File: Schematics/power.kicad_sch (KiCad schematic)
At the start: 6 parts, among them U3 PowerIn, U4 LDL1117-3.3

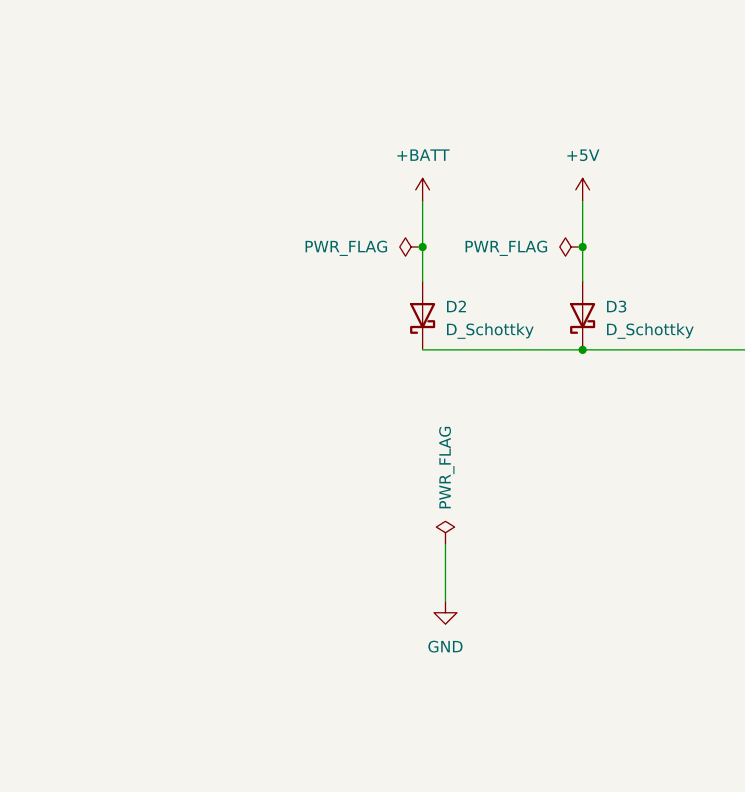
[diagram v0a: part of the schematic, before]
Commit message: added aux pyro added reverse polarity protection re routed just need to clean up and check pin assignments
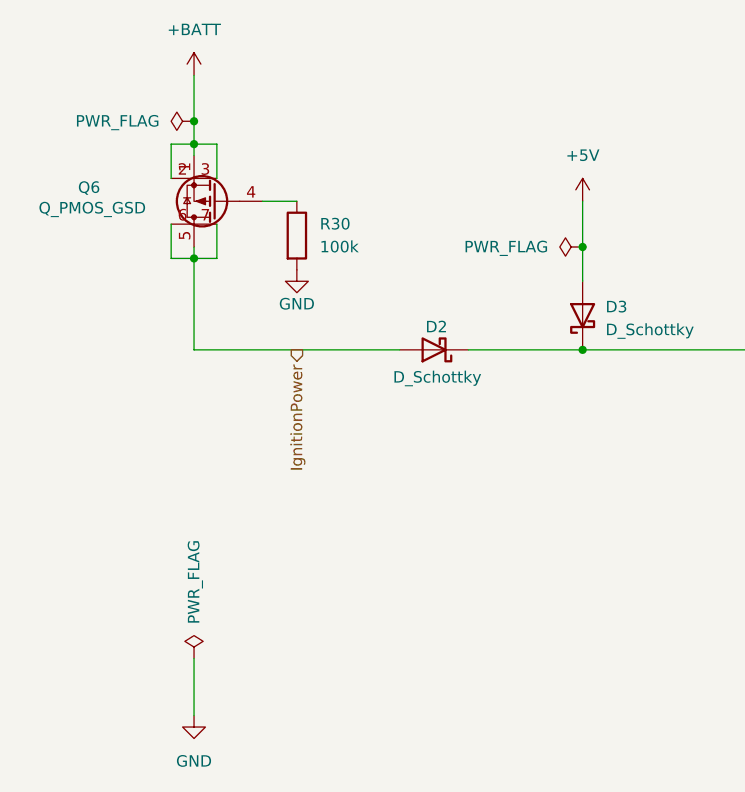
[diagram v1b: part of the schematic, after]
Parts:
- added Q6: Q_PMOS_GSD, myFootprints:SOIC127P599X175-8N, symbol Transistor_FET:Q_PMOS_SGD
- added R30: 100k, Resistor_SMD:R_0805_2012Metric_Pad1.20x1.40mm_HandSolder, symbol Device:R
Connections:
- net +BATT: now also Q6.1 (S), Q6.2 (Source), Q6.3 (Source); no longer D2.2 (A)
- net GND: now also R30.2
- new net: Q6.4 (G), R30.1
- new net IgnitionPower: D2.2 (A), Q6.5 (D), Q6.6 (Drain), Q6.7 (Drain)
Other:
- moved on the sheet: D2

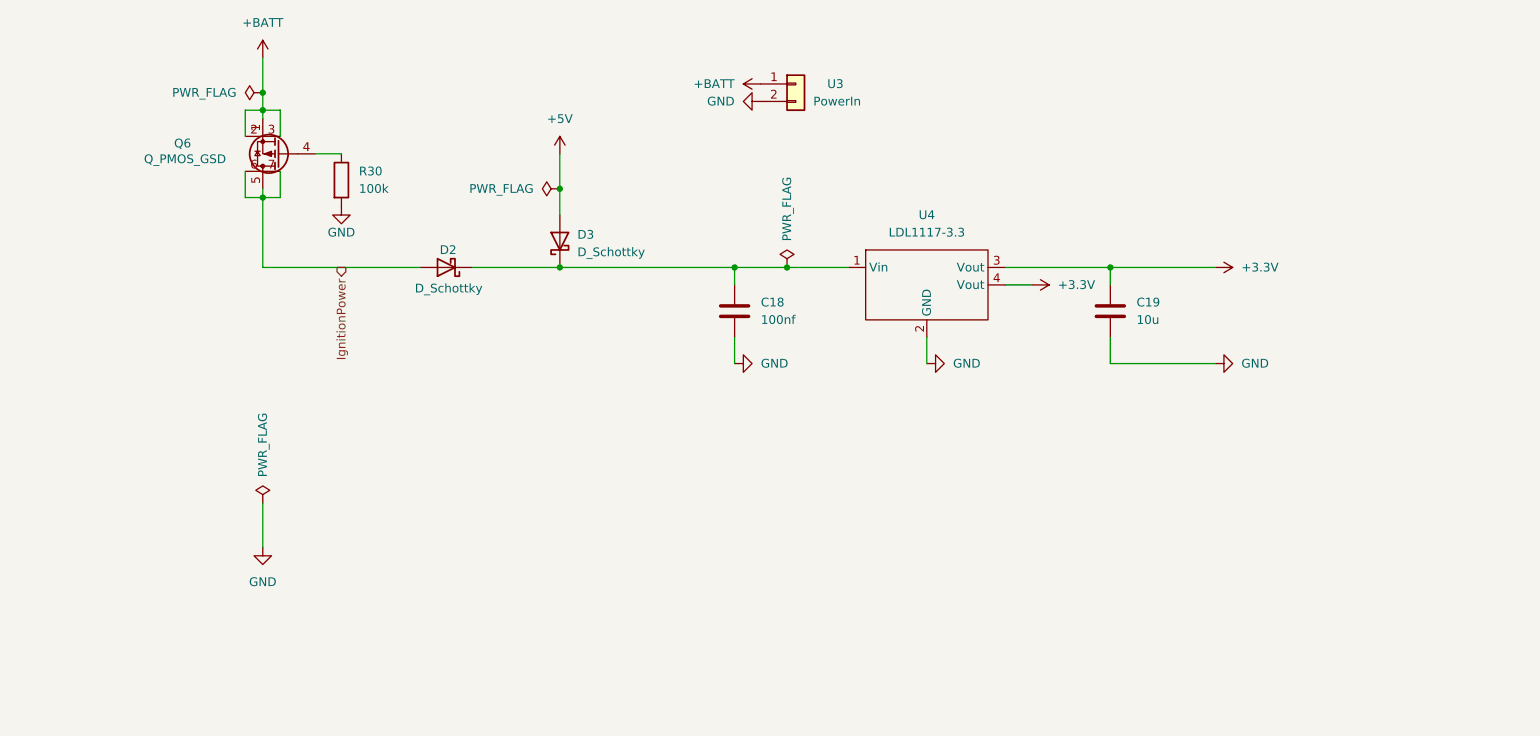
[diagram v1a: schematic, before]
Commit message: layout completed added testpoints and verified mosfet ect
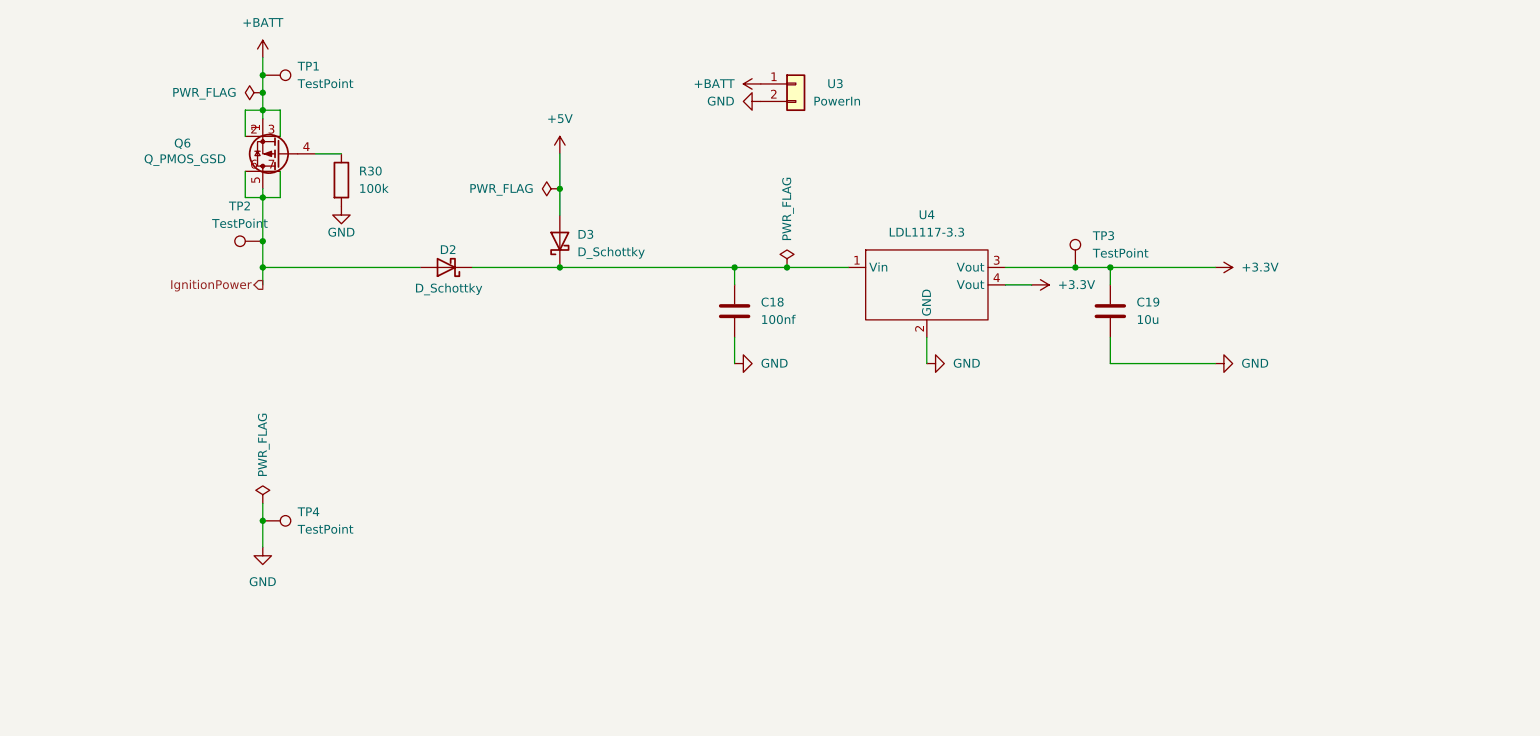
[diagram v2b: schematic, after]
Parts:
- added TP1, TP2, TP3: TestPoint, TestPoint:TestPoint_Pad_1.5x1.5mm, symbol Connector:TestPoint
- added TP4: TestPoint, TestPoint:TestPoint_Pad_2.5x2.5mm, symbol Connector:TestPoint
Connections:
- net +3.3V: now also TP3.1
- net +BATT: now also TP1.1
- net GND: now also TP4.1
- net IgnitionPower: now also TP2.1

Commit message: added comments, awaiting review
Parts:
- TP1, TP2, TP3, TP4: now left out of the parts list
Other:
- note added: "Flowback protection for usb and battery"
- note added: "P-mosfet for reverse polarity protection (be advised extra pins are there just to sync with the footprint but treated as a normal p-mosfet)"
- note added: "Power in connector"
- note added: "The main protection point for the mosfet is the adc continuty checking pins"
- moved on the sheet: C18, C19, D2, D3, Q6, R30, TP1, TP2, TP3, TP4, U3, U4
